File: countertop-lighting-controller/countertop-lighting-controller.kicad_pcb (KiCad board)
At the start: 2 copper layers, 30.5 x 12 mm, 6 parts, among them P1 CONN_01X02, P2 CONN_01X03, P3 CONN_01X03, P4 CONN_01X03, U1 ESP-01v090

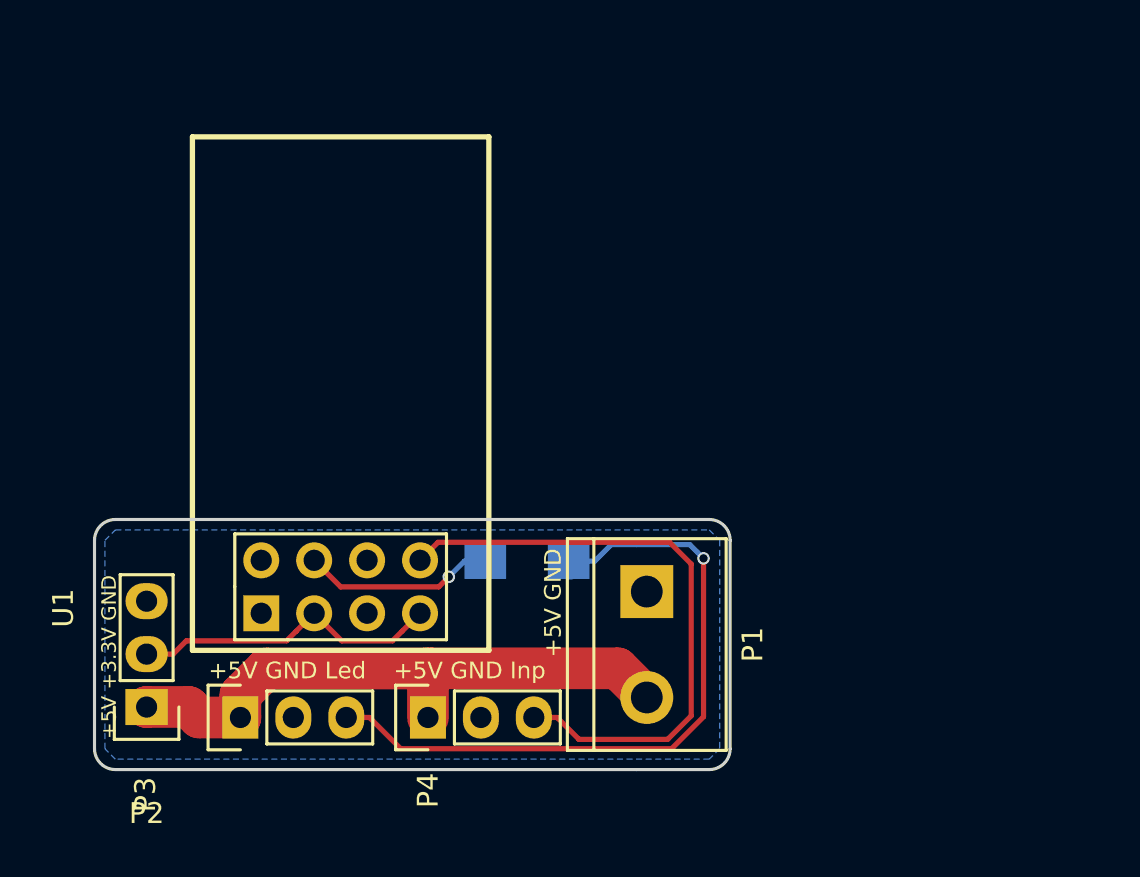
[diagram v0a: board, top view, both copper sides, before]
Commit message: Add capacitor, change button wiring, PCB
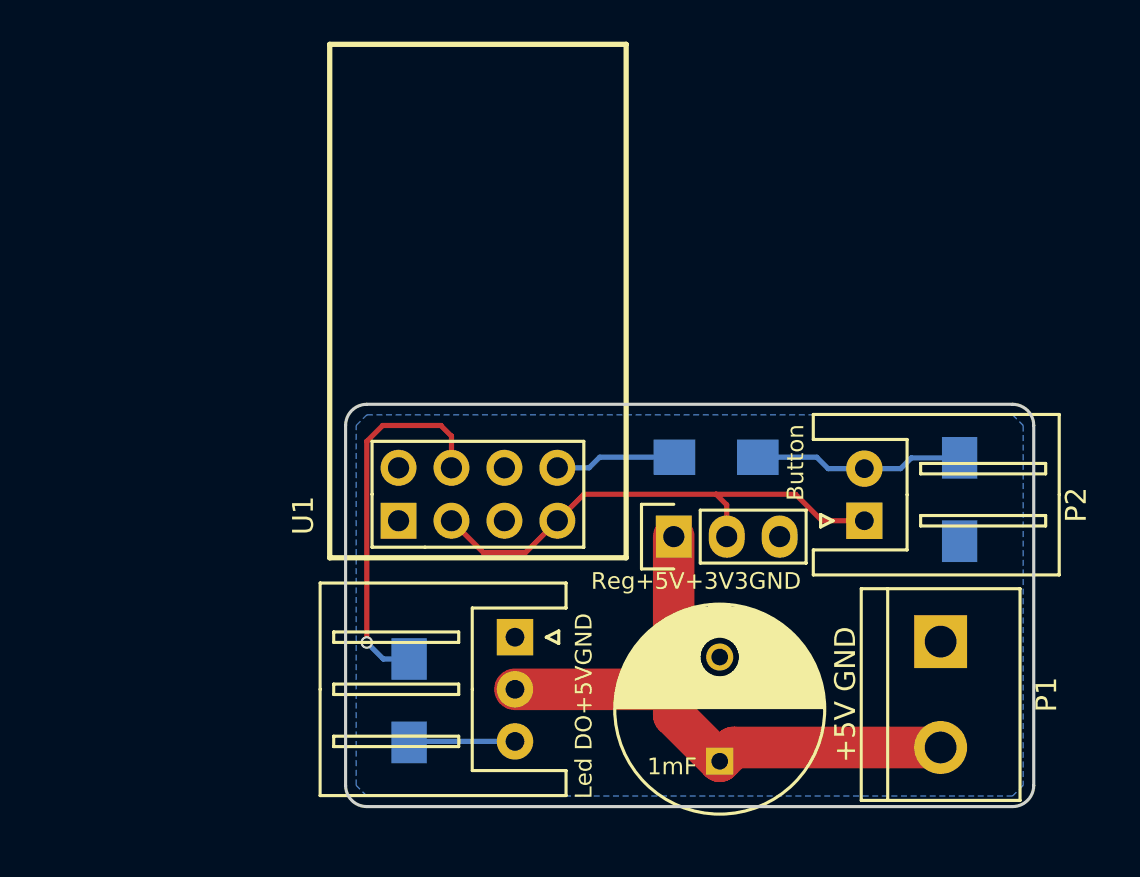
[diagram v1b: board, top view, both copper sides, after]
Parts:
- added 1mF: CP, Capacitors_ThroughHole:C_Radial_D10_L16_P5, F.Cu at (148.0, 110.6)
- added R2: 1K, Resistors_SMD:R_1206_HandSoldering, B.Cu at (147.8, 96.0)
- added R3: 10K, Resistors_SMD:R_1206_HandSoldering, B.Cu at (159.5, 98.0)
- P1: value CONN_01X02 -> +5V GND
- P2: value CONN_01X03 -> Button; footprint Pin_Headers:Pin_Header_Straight_1x03 -> Connectors_JST:JST_XH_S02B-XH-A_02x2.50mm_Angled
- P3: value CONN_01X03 -> Led DO+5VGND; footprint Pin_Headers:Pin_Header_Straight_1x03 -> Connectors_JST:JST_XH_S03B-XH-A_03x2.50mm_Angled
- P4: value CONN_01X03 -> Reg+5V+3V3GND
- R1: value R -> 470
- moved P2 35.6 mm to (154.9, 99.1), turned to 90 degrees
- moved P4 14.6 mm to (145.8, 99.8)
- moved P1 14.3 mm to (158.6, 107.4)
- moved P3 13.7 mm to (138.2, 104.6), turned to 270 degrees
- moved R1 8.76 mm to (133.1, 107.7), turned to 90 degrees
- moved U1 7.94 mm to (132.6, 99.1)
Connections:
- P2 pad 1: +5V -> +3V3
- P2 pad 2: +3V3 -> Net-(P2-Pad2)
- P3 pad 1: +5V -> GND
- P3 pad 2: GND -> +5V
- P3 pad 3: /Led -> Net-(P3-Pad3)
- P4 pad 2: GND -> +3V3
- P4 pad 3: /Input -> GND
- R1 pad 1: Net-(R1-Pad1) -> Net-(P3-Pad3)
- U1 pad 4: Net-(R1-Pad1) -> /Led
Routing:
- net /Input: track 29.5 -> 5.83 mm
- net /Led: track 33.2 -> 18.1 mm
- net Net-(P2-Pad2): track 0.00 -> 10.1 mm
- net +3V3: track 15.0 -> 24.4 mm
- net Net-(R1-Pad1): track 9.25 -> 0.00 mm, vias 1 -> 0
- net Net-(P3-Pad3): track 0.00 -> 5.10 mm
- net +5V: track 28.7 -> 30.2 mm
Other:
- board size 30.5 x 12 mm -> 33 x 19.3 mm
- board text removed: "+5V +3.3V GND"
- board text removed: "+5V GND"
- board text removed: "+5V GND Inp"
- board text removed: "+5V GND Led"
- board text removed: "Countertop"
- board text removed: "Lighting Controller"
- board text removed: "REV01"

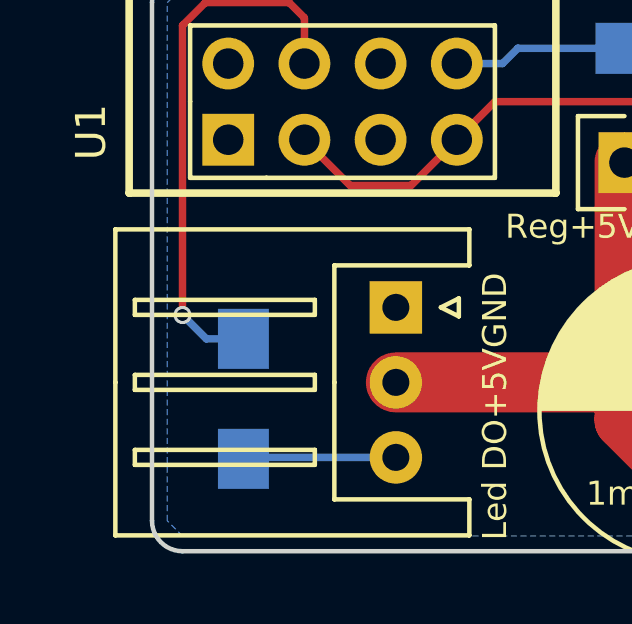
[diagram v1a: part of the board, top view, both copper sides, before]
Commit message: Update via diameter size to follow OSHPark rules
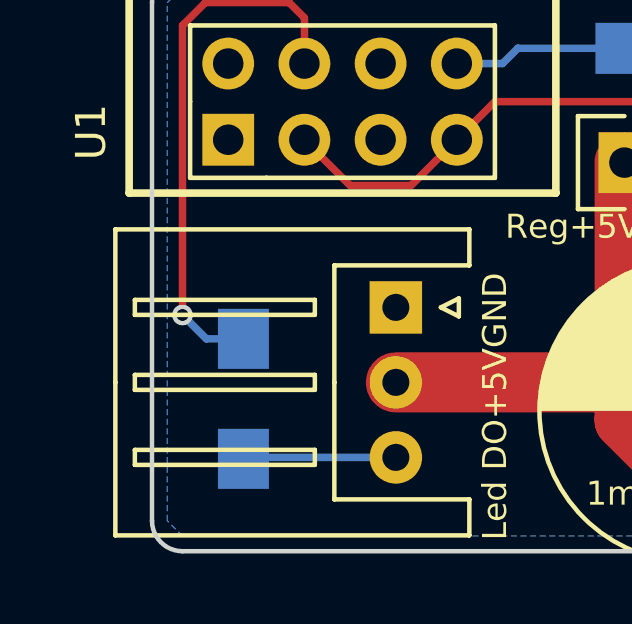
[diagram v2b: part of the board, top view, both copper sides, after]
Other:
- net class 5V: via_dia 0.6 -> 0.6858
- net class Default: via_dia 0.6 -> 0.6858
- rule trace_min: 0.2 -> 0.1524
- rule via_min_drill: 0.3 -> 0.3302
- rule via_min_size: 0.4 -> 0.6858
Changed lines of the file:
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@@
     (zone_clearance 0.508)
     (zone_45_only yes)
-    (trace_min 0.2)
+    (trace_min 0.1524)
     (segment_width 0.2)
     (edge_width 0.15)
-    (via_size 0.6)
+    (via_size 0.6858)
     (via_drill 0.4)
-    (via_min_size 0.4)
-    (via_min_drill 0.3)
+    (via_min_size 0.6858)
+    (via_min_drill 0.3302)
     (uvia_size 0.3)
     (uvia_drill 0.1)
     (uvias_allowed no)
-    (uvia_min_size 0.2)
-    (uvia_min_drill 0.1)
+    (uvia_min_size 0)
+    (uvia_min_drill 0)
     (pcb_text_width 0.3)
     (pcb_text_size 1.5 1.5)
@@
     (clearance 0.2)
     (trace_width 0.25)
-    (via_dia 0.6)
+    (via_dia 0.6858)
     (via_drill 0.4)
     (uvia_dia 0.3)
@@
     (clearance 0.2)
     (trace_width 2)
-    (via_dia 0.6)
+    (via_dia 0.6858)
     (via_drill 0.4)
     (uvia_dia 0.3)
@@
   (segment (start 133.096 105.696) (end 131.858 105.696) (width 0.25) (layer B.Cu) (net 4))
   (segment (start 131.858 105.696) (end 131.064 104.902) (width 0.25) (layer B.Cu) (net 4))
-  (via (at 131.064 104.902) (size 0.6) (drill 0.4) (layers F.Cu B.Cu) (net 4))
+  (via (at 131.064 104.902) (size 0.6858) (drill 0.4) (layers F.Cu B.Cu) (net 4))
   (segment (start 142.24 96.012) (end 141.732 96.52) (width 0.25) (layer B.Cu) (net 8))
   (segment (start 141.732 96.52) (end 140.208 96.52) (width 0.25) (layer B.Cu) (net 8))
